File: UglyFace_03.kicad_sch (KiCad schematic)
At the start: 53 parts, among them J1 9V, J2 9V GND, J3 IN, J4 IN GND, J5 OUT, J6 OUT GND, J7 LED -, J8 LED GND, U1 TL072, U2 TLC555, U3 Vactrol

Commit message: Ugly Face 3 v1.1: C4 100u, RESET 22k, filtered 555 supply, clean dry path, buffered VB, THRESHOLD toggle, GLITCH trimmer, D3/D4 LED pads
As ordered from JLCPCB (October 2026 batch).

Co-Authored-By: Claude Opus 5.5 <noreply@anthropic.com>
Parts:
- added C17: 4.7u, Capacitor_SMD:C_0805_2012Metric_Pad1.18x1.45mm_HandSolder, symbol Device:C
- added C18: 22u, Capacitor_SMD:C_1206_3216Metric_Pad1.33x1.80mm_HandSolder, symbol Device:C
- added C19: 100n, Capacitor_SMD:C_0805_2012Metric_Pad1.18x1.45mm_HandSolder, symbol Device:C
- added D3, D4: 1N4148/LED, UglyFace:D_THT_Standing_3mm_P2.54_Compact, symbol Diode:1N4148W
- added R20: 1k, Resistor_SMD:R_0805_2012Metric_Pad1.20x1.40mm_HandSolder, symbol Device:R
- added R21: 2k2, Resistor_SMD:R_0805_2012Metric_Pad1.20x1.40mm_HandSolder, symbol Device:R
- added R22: 22k, Resistor_SMD:R_0805_2012Metric_Pad1.20x1.40mm_HandSolder, symbol Device:R
- added R23: 47, Resistor_SMD:R_0805_2012Metric_Pad1.20x1.40mm_HandSolder, symbol Device:R
- added R24: 33k, Resistor_SMD:R_0805_2012Metric_Pad1.20x1.40mm_HandSolder, symbol Device:R
- added R25: 10k, Resistor_SMD:R_0805_2012Metric_Pad1.20x1.40mm_HandSolder, symbol Device:R
- added SW1: THR, UglyFace:SW_Taiway_100_SPDT_PC, symbol Switch:SW_SPDT
- added U4: TL072, Package_SO:SOIC-8_3.9x4.9mm_P1.27mm, symbol Amplifier_Operational:TL072
- C1: FT Rotation Offset (none) -> 180
- C12, C13: value 100n -> 1u; LCSC C49678 -> C28323
- C4: value 22u -> 100u; footprint Capacitor_SMD:C_1206_3216Metric_Pad1.33x1.80mm_HandSolder -> Capacitor_SMD:CP_Elec_6.3x7.7; symbol Device:C -> Device:C_Polarized; FT Rotation Offset (none) -> 180; LCSC C12891 -> C970685
- C7: value 10u -> 2.2u; LCSC C15850 -> C377773
- D2, RV1, RV3, RV4, RV5, U3: now left out of the parts list
- R13: value 15k -> 47k; LCSC C17475 -> C17713
- RV2: value B10k -> 10k; footprint UglyFace:Potentiometer_Alpha_16mm_Vertical -> UglyFace:Potentiometer_Bourns_3362P_Vertical; Panel THRESHOLD -> (none); now left out of the parts list
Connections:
- net +9V: now also C19.1, R21.1, R23.1, U4.8 (V+); no longer C3.1, U2.8 (VCC)
- net GND: now also C17.2, C18.2, C19.2, R20.2, U4.4 (V-)
- net PRE_OUT: no longer C13.1
- net RESET: now also R22.2; no longer C9.2, RV2.2
- net VB: now also U4.6 (-), U4.7; no longer C4.1, R1.2, R2.1
- net PRE_IN: now reaches C6.2, R4.2, U1.3 (+)
- net PRE_IN: now also U4.3 (+)
- new net: D3.1 (K), D4.2 (A), R24.1, R25.1, U4.2 (-)
- new net: C17.1, R25.2
- new net: R21.2, SW1.3 (C)
- new net: R20.1, SW1.1 (A)
- new net DRY_OUT: C13.1, D3.2 (A), D4.1 (K), R24.2, U4.1
- new net GATE_BIAS: C9.2, R22.1, RV2.2, SW1.2 (B)
- new net V555: C18.1, C3.1, R23.2, U2.8 (VCC)
- new net VB_RAW: C4.1, R1.2, R2.1, U4.5 (+)
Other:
- note added: "2. Hand-soldered: RV1, RV3-RV5 (Alpha 16mm), RV2 (3362P trimmer), SW1 (Taiway 100 toggle), D2 (3mm LED), U3 (DIY vactrol), J1-J8 wire pads. D3/D4 optional (3 mm LEDs / 1N4148, not fitted)."
- note added: "4. v1.1 (2026-10-03): C4 100u elec; R22 22k into RESET; C7 2.2u; R23/C18 555 supply filter; C12/C13 1u; U4A clean dry path; U4B VB buffer;"
- note added: "C7 2.2u (v1.1, was 10u): control-path LF corner ~72 Hz"
- note added: "D3/D4 not fitted: 3 mm LEDs or standing 1N4148s for a soft-clipped dry."
- note added: "GATED"
- note added: "ON"
- note added: "THRESHOLD pot -> SW1 toggle (GATED / GLITCH / ON) + RV2 3362P trimmer; R13 47k (mix balance)."
- note added: "U1A (gain 201) now drives only the gate and envelope."
- note added: "U4A: clean dry path for MIX (v1.1)."
- note added: "U4B buffers VB (MIX pot wiper and the preamp bias return here)"
- note removed: "2. Hand-soldered: RV1-RV5 (Alpha 16mm), D2 (3mm LED), U3 (DIY vactrol), J1-J8 wire pads."
- note removed: "C7 was 220n (720 Hz bass cut)"
- moved on the sheet: C3

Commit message: UF3 schematic rev 1.3: new envelope (U5 LM358 detector from DRY_OUT, Q1 vactrol current sink, DECAY trim), D6 BAT54S RESET clamp, R21 15k, R13 220k; R7/C8 removed
Co-Authored-By: Claude Opus 5.5 <noreply@anthropic.com>
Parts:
- removed C8: 100u, Capacitor_SMD:CP_Elec_6.3x7.7, symbol Device:C_Polarized
- removed R7: 100, Resistor_SMD:R_0805_2012Metric_Pad1.20x1.40mm_HandSolder, symbol Device:R
- added C20: 33n, Capacitor_SMD:C_0805_2012Metric_Pad1.18x1.45mm_HandSolder, symbol Device:C
- added C21: 1u, Capacitor_SMD:C_0805_2012Metric_Pad1.18x1.45mm_HandSolder, symbol Device:C
- added C22: 100n, Capacitor_SMD:C_0805_2012Metric_Pad1.18x1.45mm_HandSolder, symbol Device:C
- added D5: 1N4148W, Diode_SMD:D_SOD-123, symbol Diode:1N4148W
- added D6: BAT54S, Package_TO_SOT_SMD:SOT-23, symbol Diode:BAT54S
- added Q1: MMBT3904, Package_TO_SOT_SMD:SOT-23, symbol Transistor_BJT:MMBT3904
- added R26: 10k, Resistor_SMD:R_0805_2012Metric_Pad1.20x1.40mm_HandSolder, symbol Device:R
- added R27, R33: 1k, Resistor_SMD:R_0805_2012Metric_Pad1.20x1.40mm_HandSolder, symbol Device:R
- added R28: 470k, Resistor_SMD:R_0805_2012Metric_Pad1.20x1.40mm_HandSolder, symbol Device:R
- added R29, R30: 22k, Resistor_SMD:R_0805_2012Metric_Pad1.20x1.40mm_HandSolder, symbol Device:R
- added R31, R32: 100k, Resistor_SMD:R_0805_2012Metric_Pad1.20x1.40mm_HandSolder, symbol Device:R
- added R34: 330, Resistor_SMD:R_0805_2012Metric_Pad1.20x1.40mm_HandSolder, symbol Device:R
- added R35: 100, Resistor_SMD:R_0805_2012Metric_Pad1.20x1.40mm_HandSolder, symbol Device:R
- added R36: 1M, Resistor_SMD:R_0805_2012Metric_Pad1.20x1.40mm_HandSolder, symbol Device:R
- added RV6: 500k, UglyFace:Potentiometer_Bourns_3362P_Vertical, symbol Device:R_Potentiometer
- added U5: LM358, Package_SO:SOIC-8_3.9x4.9mm_P1.27mm, symbol Amplifier_Operational:LM358
- R13: value 47k -> 220k; LCSC C17713 -> C17556
- R21: value 2k2 -> 15k; LCSC C17520 -> C17475
- RV1: value B1k -> A10k
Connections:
- net +9V: now also C22.1, R31.1, R35.1, R36.1, U5.8 (V+)
- net DRY_OUT: now also C20.1
- net GND: now also C21.2, C22.2, D6.1 (A), R34.2, U5.4 (V-); no longer RV1.1, U3.2 (K)
- net RESET: now also D6.3 (COM)
- net V555: now also D6.2 (K)
- net VB: now also RV1.1, R29.2, RV6.2, RV6.3
- net at RV1.3: now also R26.2
- net VACT_LED: no longer names the net of U3.1 (A)
- net VACT_LED: now also R35.2; no longer RV1.2
- new net: D5.1 (K), R27.1
- new net: R28.1, R29.1, U5.2 (-)
- new net: R33.1, U5.7
- new net: Q1.1 (B), R33.2
- new net: Q1.3 (C), U3.2 (K)
- new net: Q1.2 (E), R32.2, R34.1
- new net: R31.2, R32.1, R36.2, U5.6 (-)
- new net: C20.2, R26.1
- new net: D5.2 (A), U5.1
- new net: RV1.2, U5.3 (+)
- new net: R30.2, RV6.1
- new net ENV: C21.1, R27.2, R28.2, R30.1, U5.5 (+)
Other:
- note added: "5. v1.3 (2026-10-16): new envelope (U5 LM358 detector + Q1 LED driver, fed from DRY_OUT; R7/C8 removed; RV1 A10k level; RV6 DECAY trim);"
- note added: "D6 BAT54S RESET clamp; R21 15k (THR ON lets the guitar through); R13 220k (MIX balance)."
- note added: "DECAY"
- note added: "I_LED = 2.1 x (ENV - VB - 0.2 V) / R34, ~15 mA max"
- note added: "LDR (U3 pins 3-4) is in parallel with FREQUENCY:"
- note added: "R36: ~0.2 V dead zone, so the LED is fully off at rest"
- note added: "U5A peak detector x22"
- note added: "VACTROL DRIVER (U5B, Q1)"
- note added: "fully down = no envelope"
- note added: "more envelope -> lower LDR R -> pitch rises"
- note added: "v1.3: from clean DRY_OUT"
- note added: "~240 Hz tilt evens strings"
- moved on the sheet: RV1, U3

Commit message: UF3 v1.3 PCB: new envelope parts placed and routed, slotted Taiway footprint, R31/R32 Basic 100k; renders, schematic PDF, docs
Board synced to schematic rev 1.3 (U5, Q1, D5, D6, C20-C22, R26-R36, RV6 added; R7, C8 removed; R13 220k, R21 15k, RV1 A10k).
Fully routed (46 vias), DRC 0 errors, parity clean. Envelope not breadboarded yet.

Co-Authored-By: Claude Opus 5.5 <noreply@anthropic.com>
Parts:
- R31, R32: LCSC C17407 -> C149504
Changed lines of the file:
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@@
 			)
 		)
-		(property "Description" "Mix input (oscillator), 47k (v1.1: was 15k) balances the 8 Vpp square against the clean dry signal"
+		(property "Description" "Mix input (oscillator): 220k (v1.3; v1.1 47k) balances the ~8 V square against the dry signal so MIX unity sits near noon"
 			(at 284.48 167.64 90)
 			(hide yes)
@@
 			)
 		)
-		(property "LCSC" "C17407"
+		(property "LCSC" "C149504"
 			(at 167.64 180.34 90)
 			(hide yes)
@@
 			)
 		)
-		(property "LCSC" "C17407"
+		(property "LCSC" "C149504"
 			(at 149.86 172.72 90)
 			(hide yes)

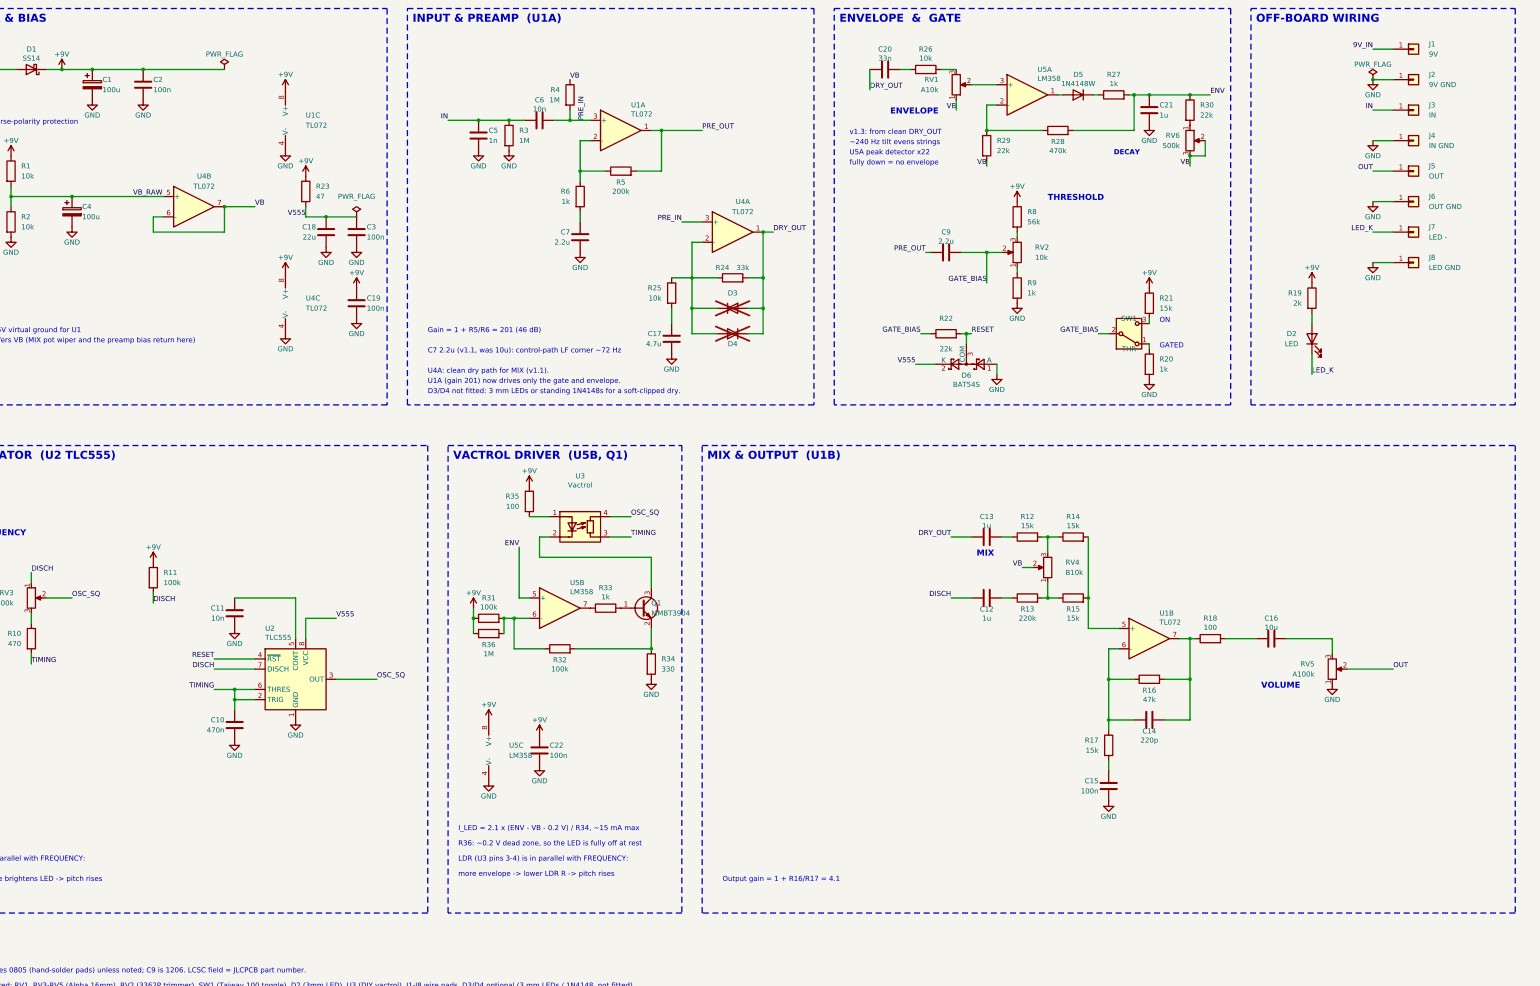
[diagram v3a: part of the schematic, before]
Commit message: v1.3 = FU-2: silk 'FU-2 v1.3', R8 47k (Basic), C21 4.7u (bench-tested envelope), schematic title; envelope breadboard sheet; docs, renders
Co-Authored-By: Claude Opus 5.5 <noreply@anthropic.com>
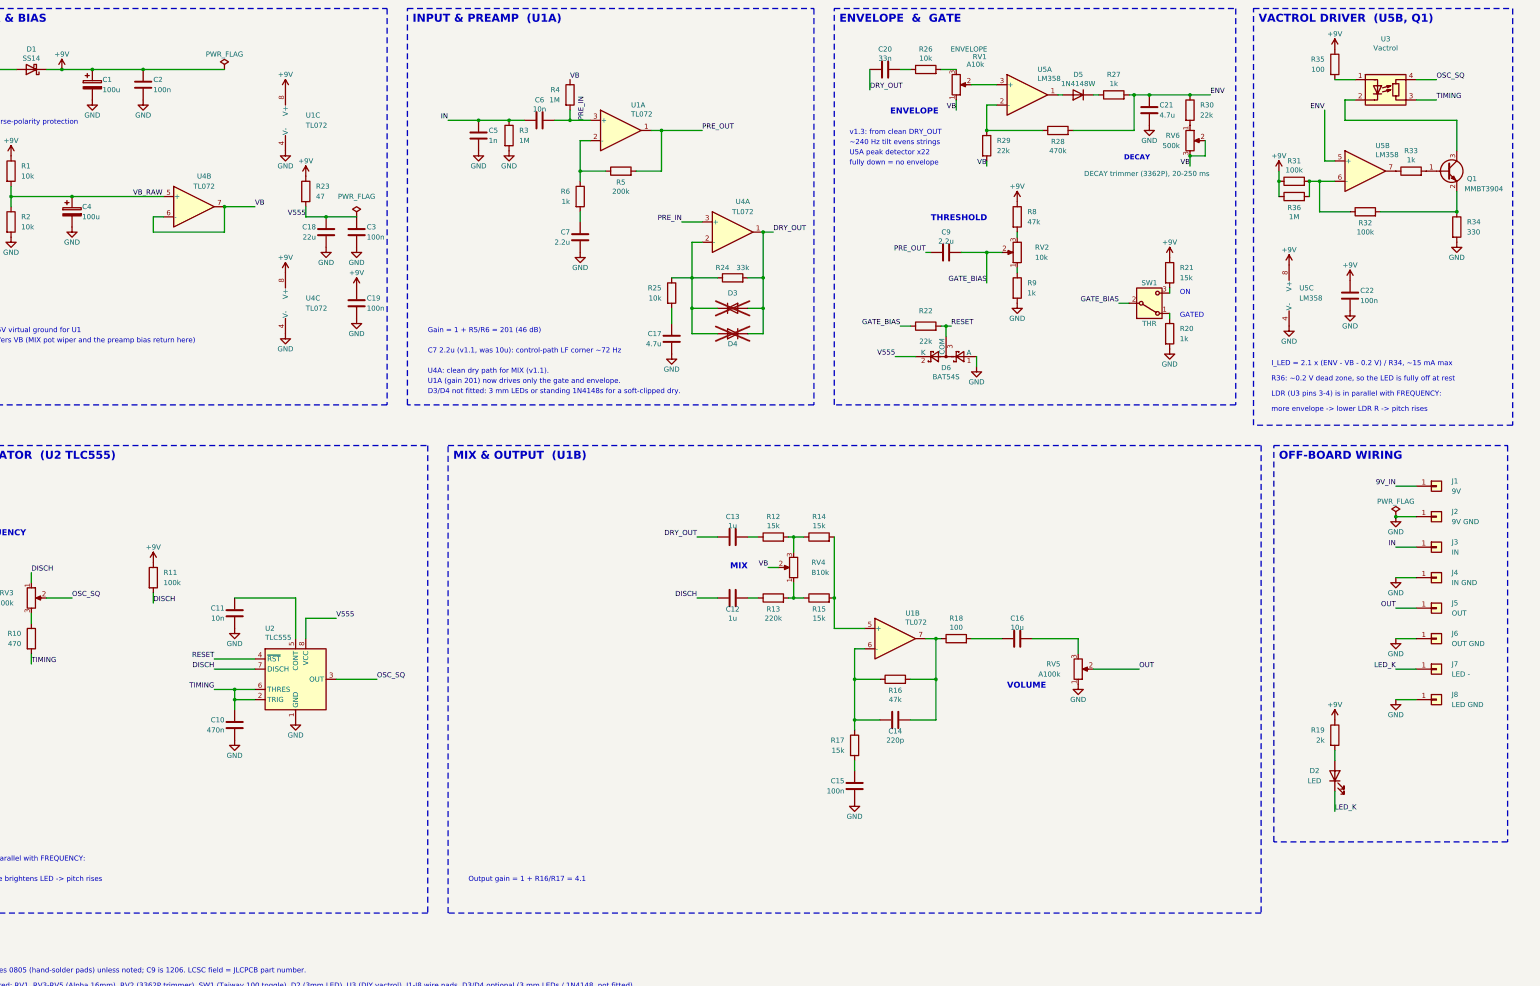
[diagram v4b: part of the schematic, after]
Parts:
- C21: value 1u -> 4.7u; LCSC C28323 -> C1779
- R8: value 56k -> 47k; LCSC C17756 -> C17713
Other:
- title: Ugly Face 3 - SMD -> FU-2 (Ugly Face 3 SMD lineage)
- moved on the sheet: C12, C13, C14, C15, C16, C22, D2, D6, J1, J2, J3, J4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
